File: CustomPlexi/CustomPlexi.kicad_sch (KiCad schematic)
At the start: 0 parts

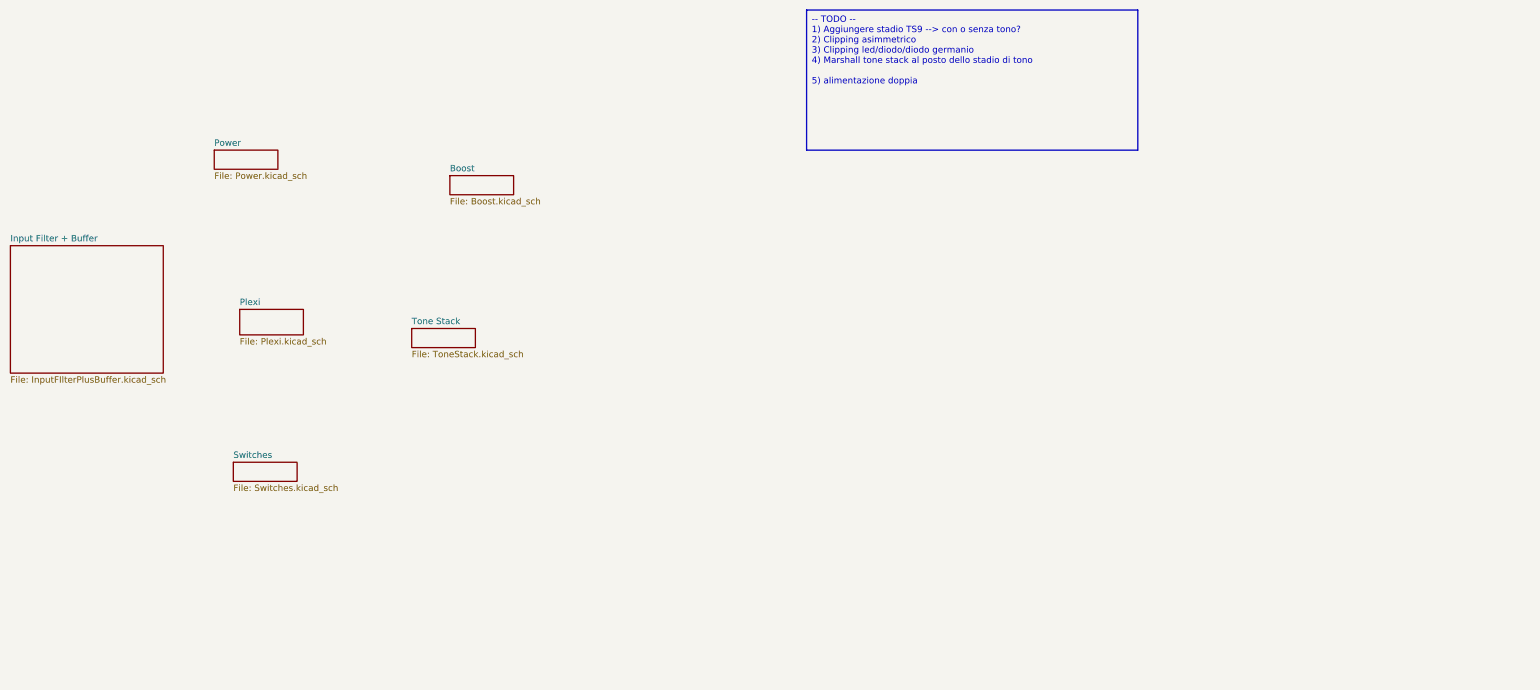
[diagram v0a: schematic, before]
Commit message: Signal chain ok except separated volumes
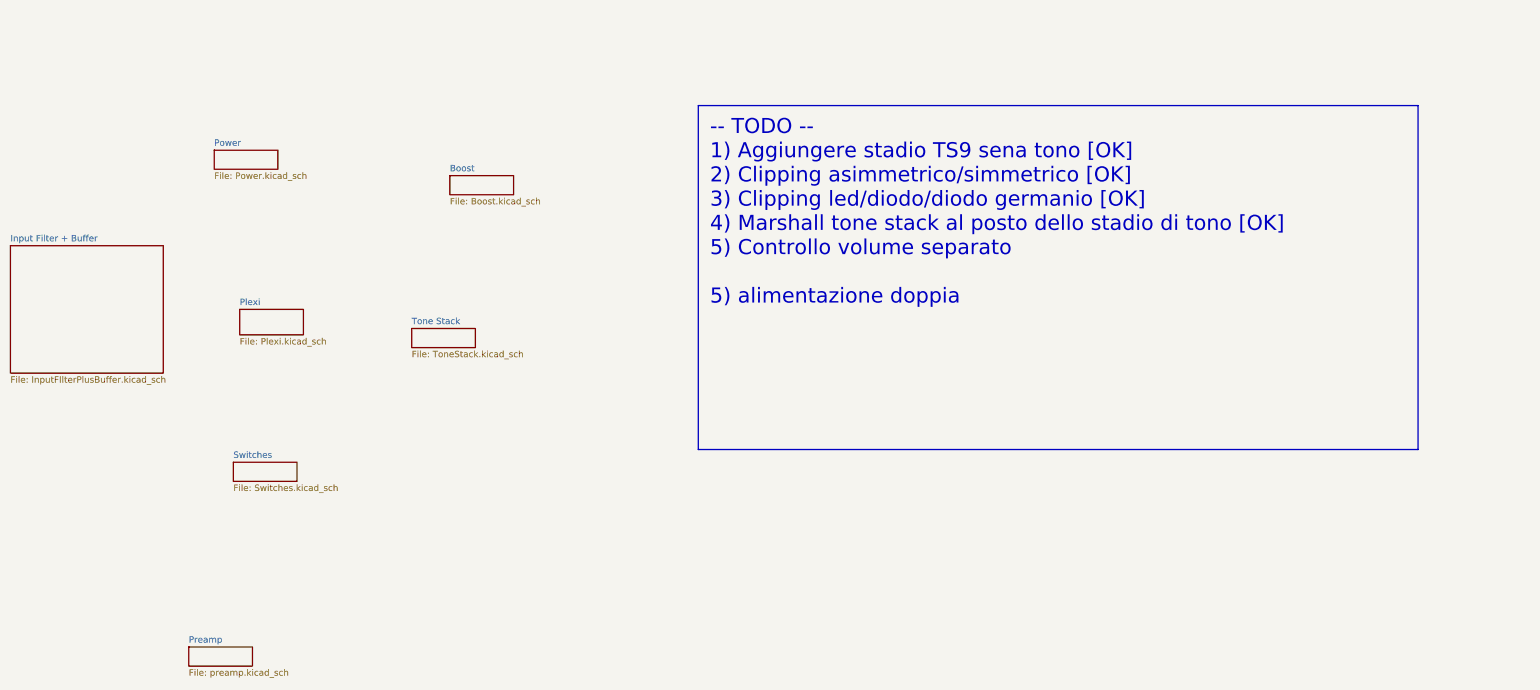
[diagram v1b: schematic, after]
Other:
- added sheet Preamp (preamp.kicad_sch)
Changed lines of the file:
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@@
     (rev "Rev0")
   )
-  (text_box "-- TODO --\n1) Aggiungere stadio TS9 --> con o senza tono?\n2) Clipping asimmetrico\n3) Clipping led/diodo/diodo germanio\n4) Marshall tone stack al posto dello stadio di tono\n\n5) alimentazione doppia"
-    (at 207.01 17.78 0) (size 66.04 27.94)
+  (text_box "-- TODO --\n1) Aggiungere stadio TS9 sena tono [OK]\n2) Clipping asimmetrico/simmetrico [OK]\n3) Clipping led/diodo/diodo germanio [OK]\n4) Marshall tone stack al posto dello stadio di tono [OK]\n5) Controllo volume separato\n\n5) alimentazione doppia"
+    (at 185.42 36.83 0) (size 143.51 68.58)
     (stroke (width 0) (type default))
     (fill (type none))
-    (effects (font (size 1.27 1.27)) (justify left top))
+    (effects (font (size 3 3)) (justify left top))
   )
   (sheet (at 135.89 50.8) (size 12.7 3.81) (fields_autoplaced)
@@
       )
     )
+  )
+  (sheet (at 83.82 144.78) (size 12.7 3.81) (fields_autoplaced)
+    (stroke (width 0.1524) (type solid))
+    (fill (color 0 0 0 0.0000))
+    (property "Sheetname" "Preamp" (at 83.82 144.0684 0)
+      (effects (font (size 1.27 1.27)) (justify left bottom))
+    )
+    (property "Sheetfile" "preamp.kicad_sch" (at 83.82 149.1746 0)
+      (effects (font (size 1.27 1.27)) (justify left top))
+    )
+    (property "Field2" "" (at 83.82 144.78 0)
+      (effects (font (size 1.27 1.27)) hide)
+    )
+    (instances
+      (project "CustomPlexi"
+        (path "/cb47f45c-6a2b-402e-a3a9-bf4992e06e45" (page "3"))
+      )
+    )

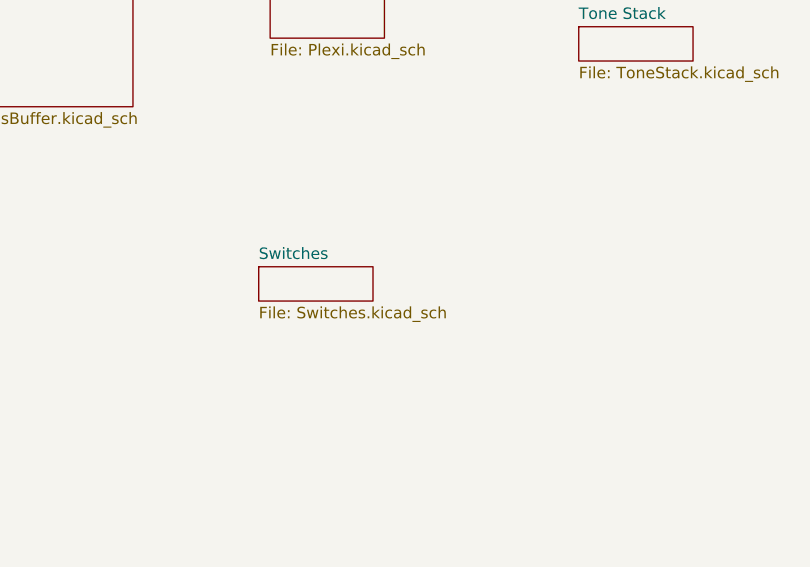
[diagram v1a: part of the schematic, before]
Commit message: crunch and leadh channel has separated level control
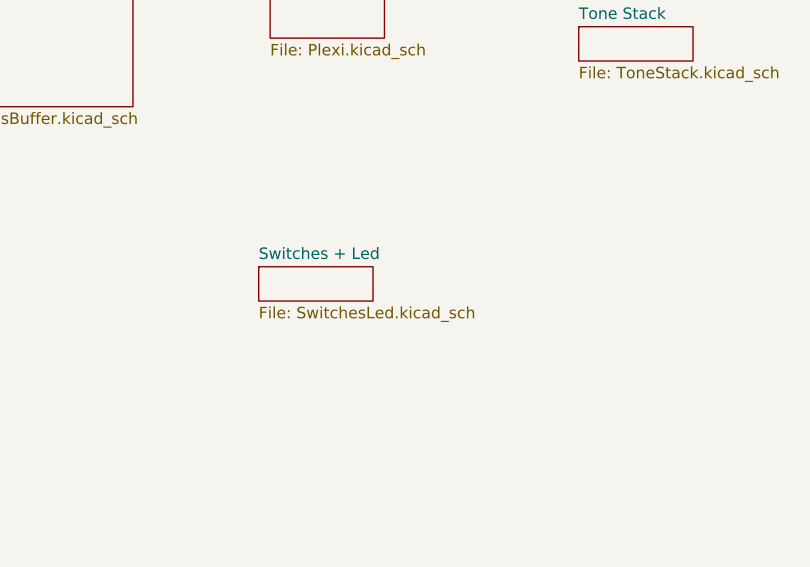
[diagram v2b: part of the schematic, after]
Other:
- sheet Switches renamed Switches + Led
- sheet Switches + Led: file Switches.kicad_sch -> SwitchesLed.kicad_sch
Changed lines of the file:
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@@
     (stroke (width 0.1524) (type solid))
     (fill (color 0 0 0 0.0000))
-    (property "Sheetname" "Switches" (at 92.71 107.2384 0)
+    (property "Sheetname" "Switches + Led" (at 92.71 107.2384 0)
       (effects (font (size 1.27 1.27)) (justify left bottom))
     )
-    (property "Sheetfile" "Switches.kicad_sch" (at 92.71 112.3446 0)
+    (property "Sheetfile" "SwitchesLed.kicad_sch" (at 92.71 112.3446 0)
       (effects (font (size 1.27 1.27)) (justify left top))
     )

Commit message: switches reviewed
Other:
- sheet Switches + Led renamed Leds
- sheet Leds: file SwitchesLed.kicad_sch -> Leds.kicad_sch
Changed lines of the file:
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@@
     (stroke (width 0.1524) (type solid))
     (fill (color 0 0 0 0.0000))
-    (property "Sheetname" "Switches + Led" (at 92.71 107.2384 0)
+    (property "Sheetname" "Leds" (at 92.71 107.2384 0)
       (effects (font (size 1.27 1.27)) (justify left bottom))
     )
-    (property "Sheetfile" "SwitchesLed.kicad_sch" (at 92.71 112.3446 0)
+    (property "Sheetfile" "Leds.kicad_sch" (at 92.71 112.3446 0)
       (effects (font (size 1.27 1.27)) (justify left top))
     )
